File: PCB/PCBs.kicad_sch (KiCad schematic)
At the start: 8 parts, among them U1 ADS1299IPAGR

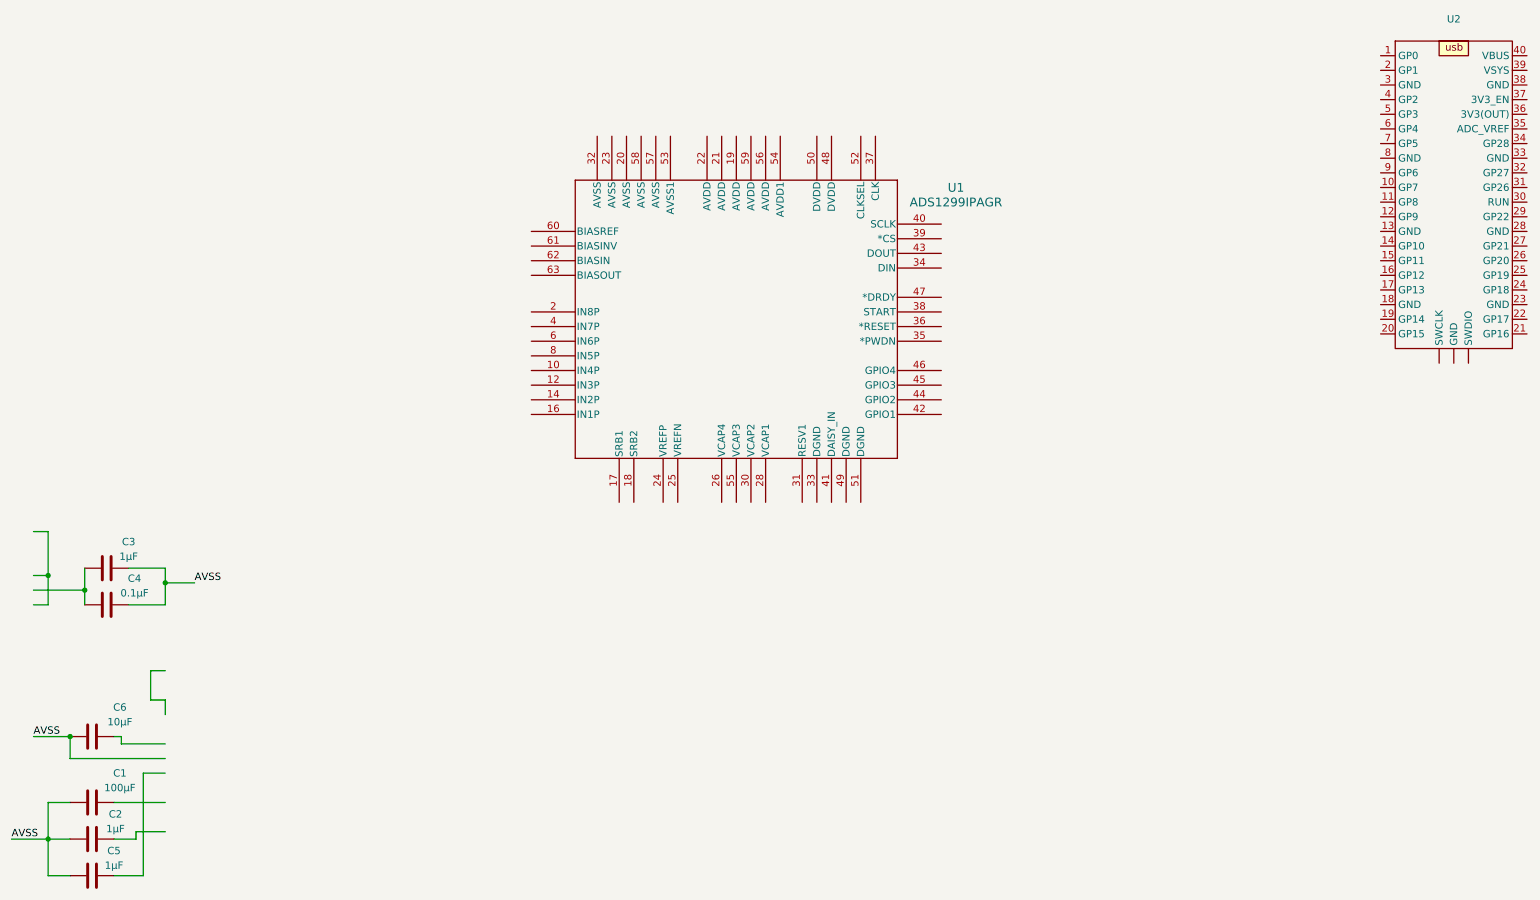
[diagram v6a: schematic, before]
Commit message: adding back INxN channels
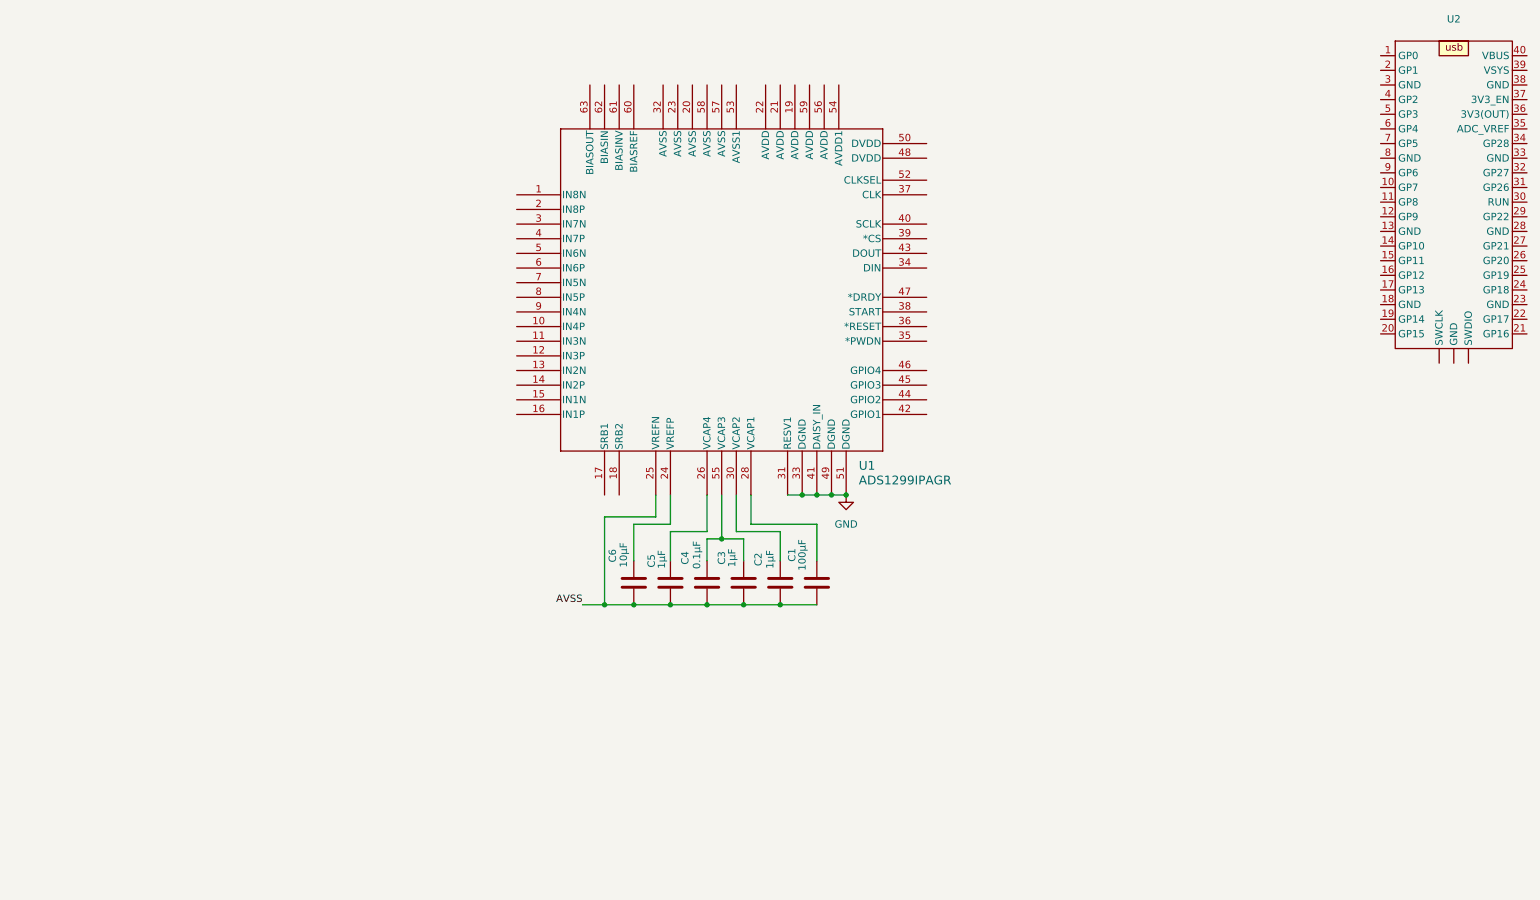
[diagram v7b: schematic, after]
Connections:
- net AVSS: now also U1.25 (VREFN)
- net at C5.1: now also U1.26 (VCAP4)
- net at C1.1: now also U1.28 (VCAP1)
- net at C3.2, C4.2: now also U1.55 (VCAP3)
- net at C2.1: now also U1.30 (VCAP2)
- net at U1.24 (VREFP): now also C6.1
- net GND: now reaches U1.31 (RESV1)
- net GND: now also U1.33 (DGND), U1.41 (DAISY_IN), U1.49 (DGND), U1.51 (DGND)
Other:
- moved on the sheet: C1, C2, C3, C4, C5, C6

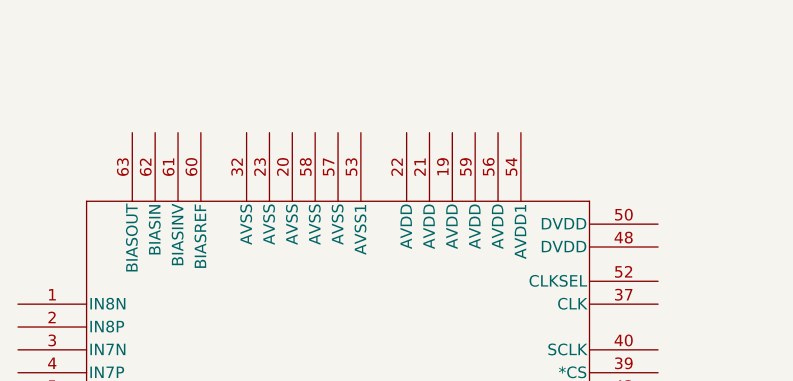
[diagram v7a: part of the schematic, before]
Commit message: avss avdd connections
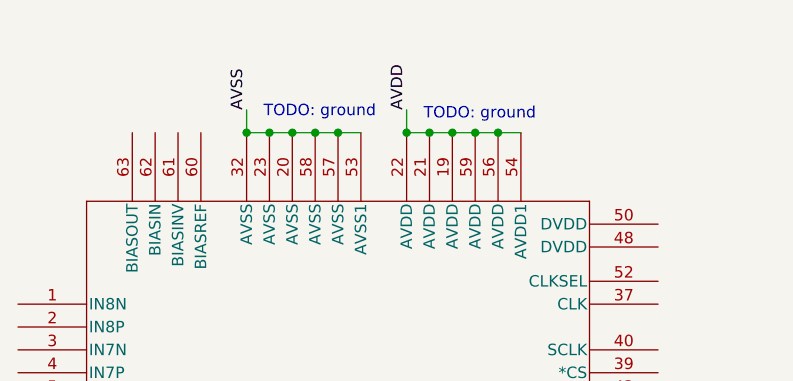
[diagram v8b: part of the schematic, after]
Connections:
- net AVSS: now also U1.20 (AVSS), U1.23 (AVSS), U1.32 (AVSS), U1.53 (AVSS1), U1.57 (AVSS), U1.58 (AVSS)
- net AVDD: now reaches U1.19 (AVDD)
- net AVDD: now also U1.21 (AVDD), U1.22 (AVDD), U1.54 (AVDD1), U1.56 (AVDD), U1.59 (AVDD)
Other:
- note added: "TODO: ground"
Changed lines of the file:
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@@
+	)
+	(junction
+		(at 137.16 55.88)
+		(diameter 0)
+		(color 0 0 0 0)
 	)
 	(junction
@@
 	)
 	(junction
+		(at 142.24 55.88)
+		(diameter 0)
+		(color 0 0 0 0)
+	)
+	(junction
 		(at 142.24 134.62)
 		(diameter 0)
@@
 	)
 	(junction
+		(at 134.62 55.88)
+		(diameter 0)
+		(color 0 0 0 0)
+	)
+	(junction
 		(at 146.05 146.05)
 		(diameter 0)
@@
 	)
 	(junction
+		(at 157.48 55.88)
+		(diameter 0)
+		(color 0 0 0 0)
+	)
+	(junction
 		(at 158.75 127)
 		(diameter 0)
@@
 	)
 	(junction
+		(at 139.7 55.88)
+		(diameter 0)
+		(color 0 0 0 0)
+	)
+	(junction
 		(at 127 146.05)
 		(diameter 0)
@@
 	)
 	(junction
+		(at 154.94 55.88)
+		(diameter 0)
+		(color 0 0 0 0)
+	)
+	(junction
+		(at 132.08 55.88)
+		(diameter 0)
+		(color 0 0 0 0)
+	)
+	(junction
 		(at 133.35 146.05)
 		(diameter 0)
 		(color 0 0 0 0)
 	)
+	(junction
+		(at 149.86 55.88)
+		(diameter 0)
+		(color 0 0 0 0)
+	)
+	(junction
+		(at 152.4 55.88)
+		(diameter 0)
+		(color 0 0 0 0)
+	)
+	(junction
+		(at 160.02 55.88)
+		(diameter 0)
+		(color 0 0 0 0)
+	)
 	(wire
 		(pts
@@
 	(wire
 		(pts
+			(xy 139.7 55.88) (xy 142.24 55.88)
+		)
+		(stroke
+			(width 0)
+			(type default)
+		)
+	)
+	(wire
+		(pts
 			(xy 133.35 133.35) (xy 133.35 138.43)
 		)
@@
 	(wire
 		(pts
+			(xy 157.48 55.88) (xy 160.02 55.88)
+		)
+		(stroke
+			(width 0)
+			(type default)
+		)
+	)
+	(wire
+		(pts
 			(xy 142.24 134.62) (xy 146.05 134.62)
 		)
@@
 	(wire
 		(pts
+			(xy 132.08 53.34) (xy 132.08 55.88)
+		)
+		(stroke
+			(width 0)
+			(type default)
+		)
+	)
+	(wire
+		(pts
+			(xy 142.24 55.88) (xy 144.78 55.88)
+		)
+		(stroke
+			(width 0)
+			(type default)
+		)
+	)
+	(wire
+		(pts
+			(xy 134.62 55.88) (xy 137.16 55.88)
+		)
+		(stroke
+			(width 0)
+			(type default)
+		)
+	)
+	(wire
+		(pts
+			(xy 160.02 55.88) (xy 162.56 55.88)
+		)
+		(stroke
+			(width 0)
+			(type default)
+		)
+	)
+	(wire
+		(pts
 			(xy 158.75 127) (xy 161.29 127)
 		)
@@
 	(wire
 		(pts
+			(xy 152.4 55.88) (xy 154.94 55.88)
+		)
+		(stroke
+			(width 0)
+			(type default)
+		)
+	)
+	(wire
+		(pts
 			(xy 142.24 127) (xy 142.24 134.62)
 		)
@@
 	(wire
 		(pts
+			(xy 137.16 55.88) (xy 139.7 55.88)
+		)
+		(stroke
+			(width 0)
+			(type default)
+		)
+	)
+	(wire
+		(pts
 			(xy 139.7 133.35) (xy 133.35 133.35)
 		)
@@
 	(wire
 		(pts
+			(xy 149.86 53.34) (xy 149.86 55.88)
+		)
+		(stroke
+			(width 0)
+			(type default)
+		)
+	)
+	(wire
+		(pts
 			(xy 152.4 146.05) (xy 158.75 146.05)
 		)
@@
 	(wire
 		(pts
+			(xy 154.94 55.88) (xy 157.48 55.88)
+		)
+		(stroke
+			(width 0)
+			(type default)
+		)
+	)
+	(wire
+		(pts
 			(xy 133.35 127) (xy 133.35 132.08)
 		)
@@
 	(wire
 		(pts
+			(xy 132.08 55.88) (xy 134.62 55.88)
+		)
+		(stroke
+			(width 0)
+			(type default)
+		)
+	)
+	(wire
+		(pts
 			(xy 161.29 127) (xy 163.83 127)
 		)
@@
 	(wire
 		(pts
+			(xy 149.86 55.88) (xy 152.4 55.88)
+		)
+		(stroke
+			(width 0)
+			(type default)
+		)
+	)
+	(wire
+		(pts
 			(xy 156.21 127) (xy 158.75 127)
 		)
@@
 		)
 	)
+	(text "TODO: ground\n"
+		(exclude_from_sim no)
+		(at 140.208 53.594 0)
+		(effects
+			(font
+				(size 1.27 1.27)
+			)
+		)
+	)
+	(text "TODO: ground\n"
+		(exclude_from_sim no)
+		(at 157.988 53.848 0)
+		(effects
+			(font
+				(size 1.27 1.27)
+			)
+		)
+	)
+	(label "AVDD"
+		(at 149.86 53.34 90)
+		(fields_autoplaced yes)
+		(effects
+			(font
+				(size 1.27 1.27)
+			)
+			(justify left bottom)
+		)
+	)
+	(label "AVSS"
+		(at 132.08 53.34 90)
+		(fields_autoplaced yes)
+		(effects
+			(font
+				(size 1.27 1.27)
+			)
+			(justify left bottom)
+		)
+	)
